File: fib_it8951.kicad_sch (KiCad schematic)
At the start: 0 parts

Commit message: added several ICs, implementted schematics for charger, boost converter and LDOs
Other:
- note added: "COONNECTOR"
- note added: "FLASH"
- note added: "HDMI->PARALLEL"
- note added: "IT8951"
- note added: "PMIC"
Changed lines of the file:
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@@
 	(generator_version "8.0")
 	(paper "A4")
+	(text "FLASH"
+		(exclude_from_sim no)
+		(at 41.91 55.372 0)
+		(effects
+			(font
+				(size 1.27 1.27)
+			)
+		)
+	)
+	(text "PMIC"
+		(exclude_from_sim no)
+		(at 41.148 44.704 0)
+		(effects
+			(font
+				(size 1.27 1.27)
+			)
+		)
+	)
+	(text "COONNECTOR"
+		(exclude_from_sim no)
+		(at 45.466 67.31 0)
+		(effects
+			(font
+				(size 1.27 1.27)
+			)
+		)
+	)
+	(text "IT8951"
+		(exclude_from_sim no)
+		(at 41.91 35.56 0)
+		(effects
+			(font
+				(size 1.27 1.27)
+			)
+		)
+	)
+	(text "HDMI->PARALLEL"
+		(exclude_from_sim no)
+		(at 47.498 79.248 0)
+		(effects
+			(font
+				(size 1.27 1.27)
+			)
+		)
+	)
 )

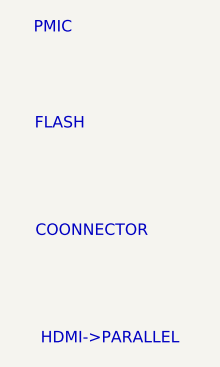
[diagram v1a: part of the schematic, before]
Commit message: added usb+PD+DP & pcie implementations from antmicro design, added specs for USB components, rethought power+usb arch
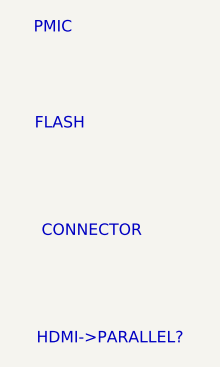
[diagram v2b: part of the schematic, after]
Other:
- note added: "CONNECTOR"
- note added: "HDMI->PARALLEL?"
- note removed: "COONNECTOR"
- note removed: "HDMI->PARALLEL"
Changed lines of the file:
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@@
 		)
 	)
-	(text "COONNECTOR"
+	(text "CONNECTOR"
 		(exclude_from_sim no)
 		(at 45.466 67.31 0)
@@
 		)
 	)
-	(text "HDMI->PARALLEL"
+	(text "HDMI->PARALLEL?"
 		(exclude_from_sim no)
 		(at 47.498 79.248 0)

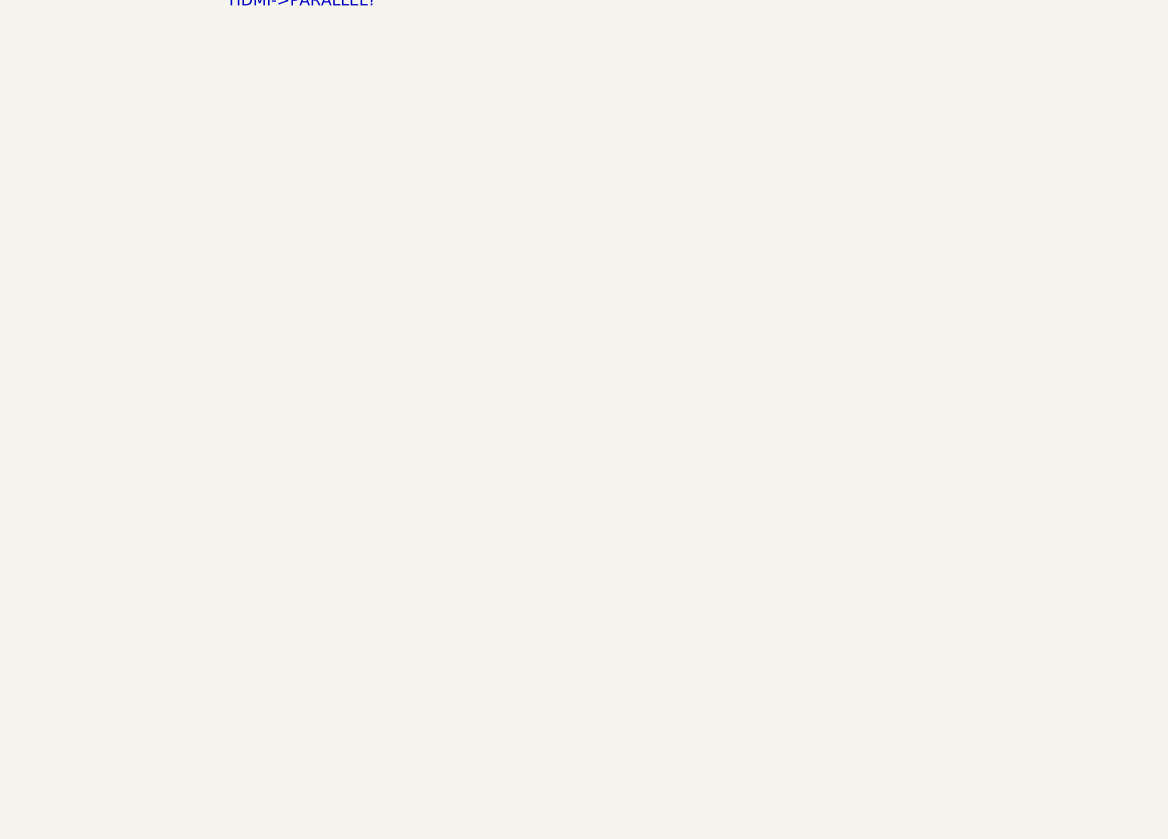
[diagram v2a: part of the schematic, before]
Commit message: added nets for 40 pin headers (epd & rpi header) connected some of the nets i'm reeusing
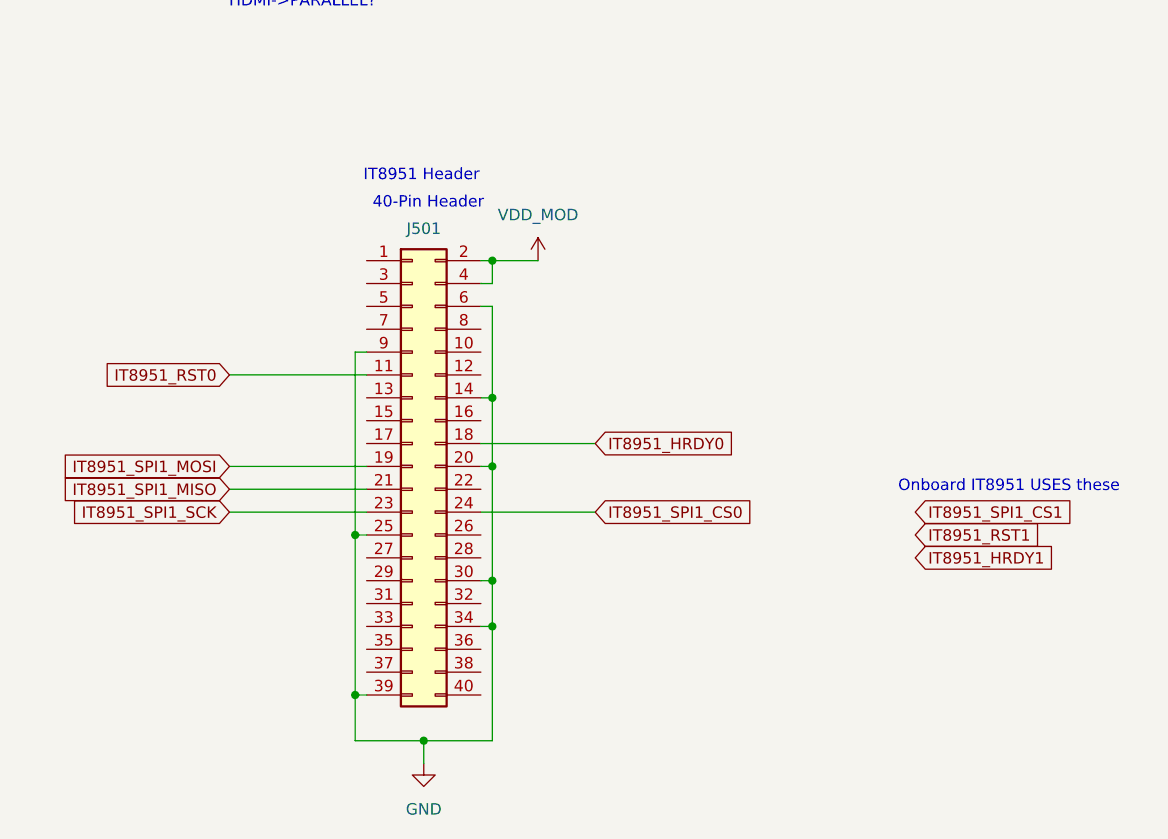
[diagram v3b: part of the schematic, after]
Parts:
- added J501: Conn_02x20_Odd_Even, Connector_PinHeader_2.54mm:PinHeader_2x20_P2.54mm_Vertical, symbol Connector_Generic:Conn_02x20_Odd_Even
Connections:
- new net GND: J501.14 (Pin_14), J501.20 (Pin_20), J501.25 (Pin_25), J501.30 (Pin_30), J501.34 (Pin_34), J501.39 (Pin_39), J501.6 (Pin_6), J501.9 (Pin_9)
- new net IT8951_HRDY0: J501.18 (Pin_18)
- new net IT8951_RST0: J501.11 (Pin_11)
- new net IT8951_SPI1_CS0: J501.24 (Pin_24)
- new net IT8951_SPI1_MISO: J501.21 (Pin_21)
- new net IT8951_SPI1_MOSI: J501.19 (Pin_19)
- new net IT8951_SPI1_SCK: J501.23 (Pin_23)
- new net VDD_MOD: J501.2 (Pin_2), J501.4 (Pin_4)
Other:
- note added: "40-Pin Header"
- note added: "IT8951 Header"
- note added: "Onboard IT8951 USES these"

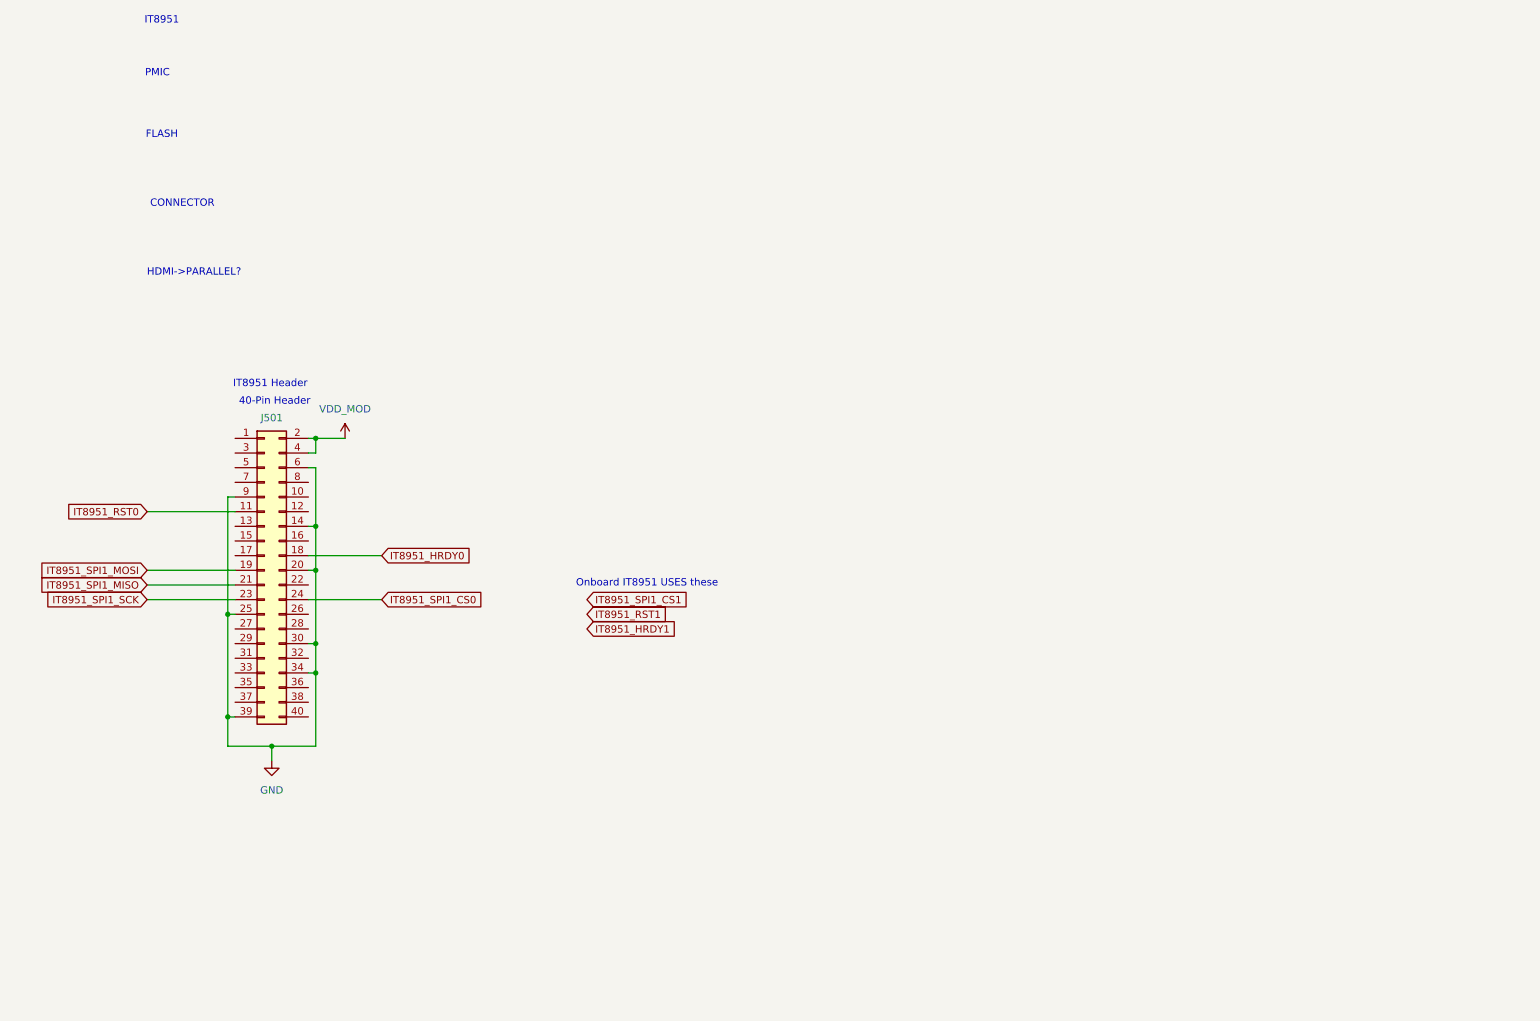
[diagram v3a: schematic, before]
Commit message: restructured EPD side of things, replaced rp2040 with esp32 s3 because of it's LCD controller, USB, LP WIFI_BT & EPDiy compat, repurposed USB0 for ESP interfacing, added e-ink pmic
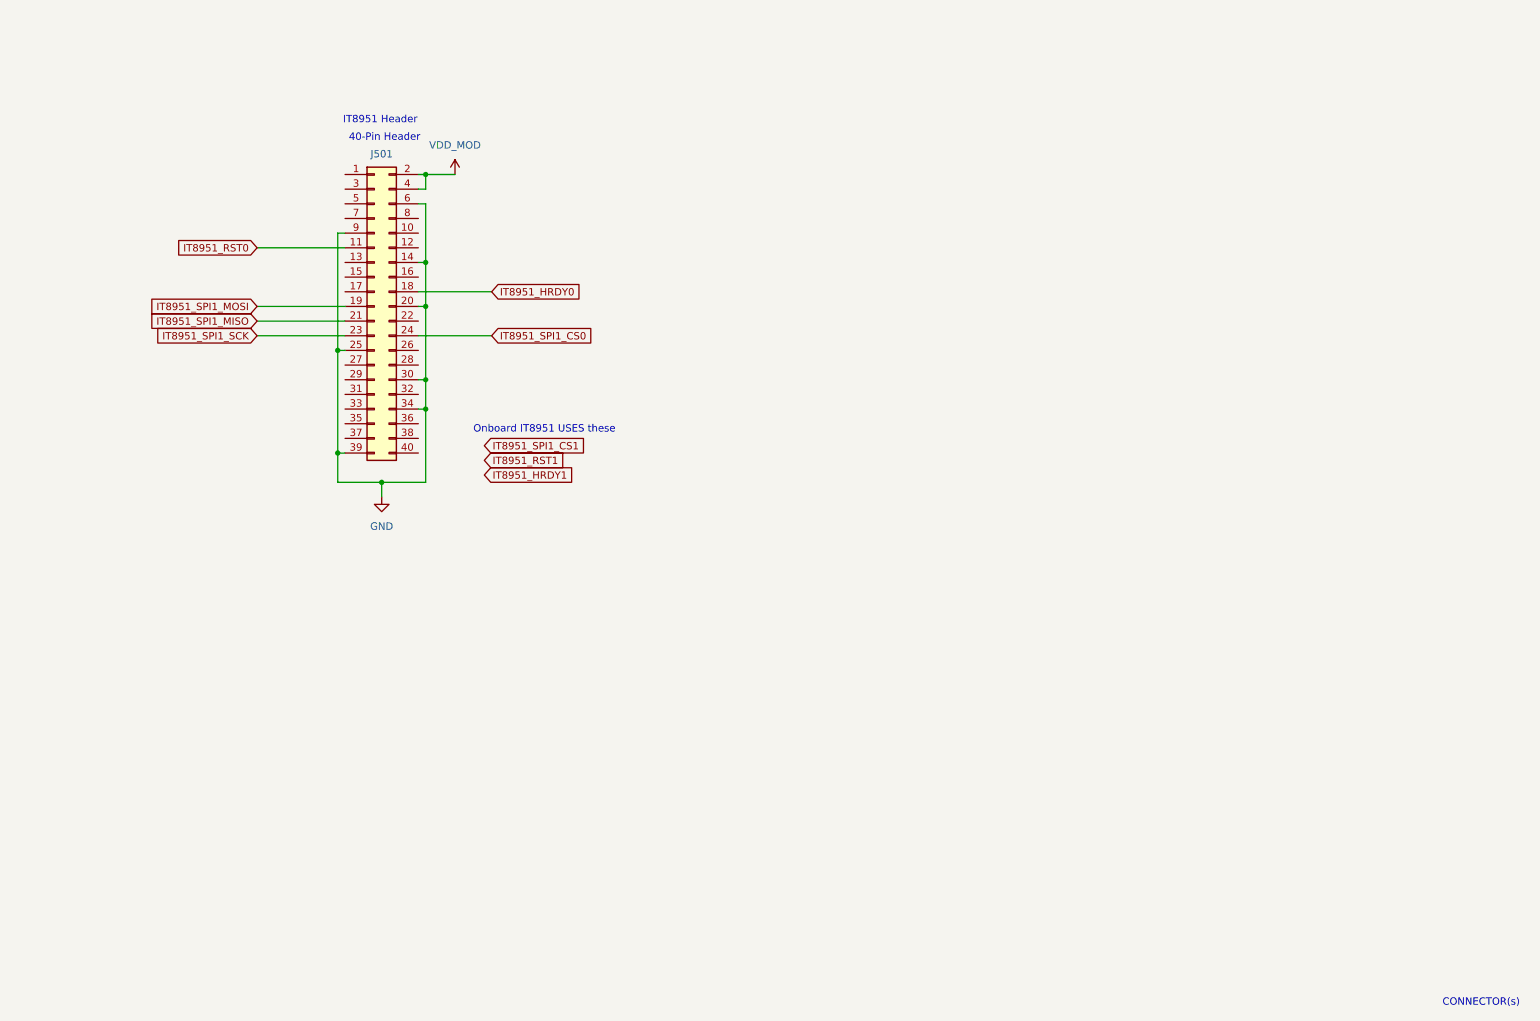
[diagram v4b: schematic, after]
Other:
- note added: "CONNECTOR(s)"
- note removed: "CONNECTOR"
- note removed: "FLASH"
- note removed: "HDMI->PARALLEL?"
- note removed: "IT8951"
- note removed: "PMIC"
- moved on the sheet: J501
